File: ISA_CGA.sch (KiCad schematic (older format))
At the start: 15 parts, among them U1 74S112, U12 74LS393, U13 74LS08, U14 74LS32, U28 74LS10, U29 74S04, U3 74S86, U30 74LS32, U31 74S08, U42 74LS86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

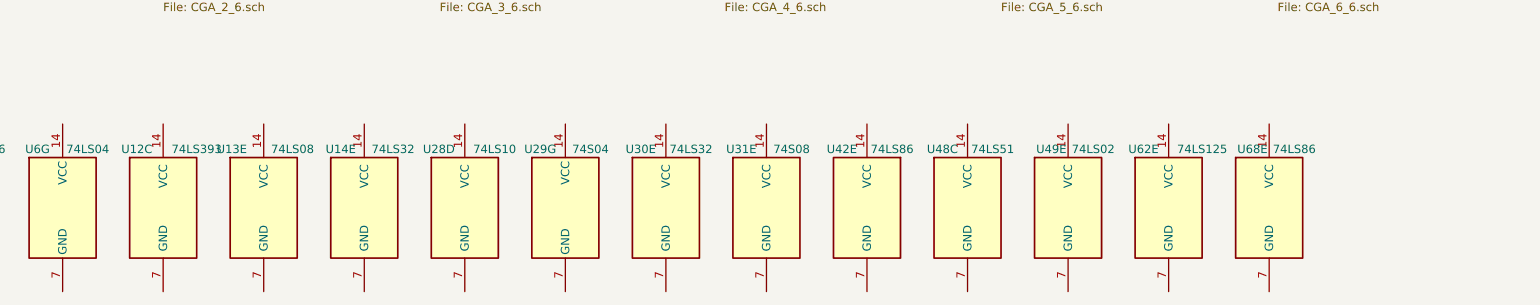
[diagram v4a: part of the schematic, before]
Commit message: Power connection for more units
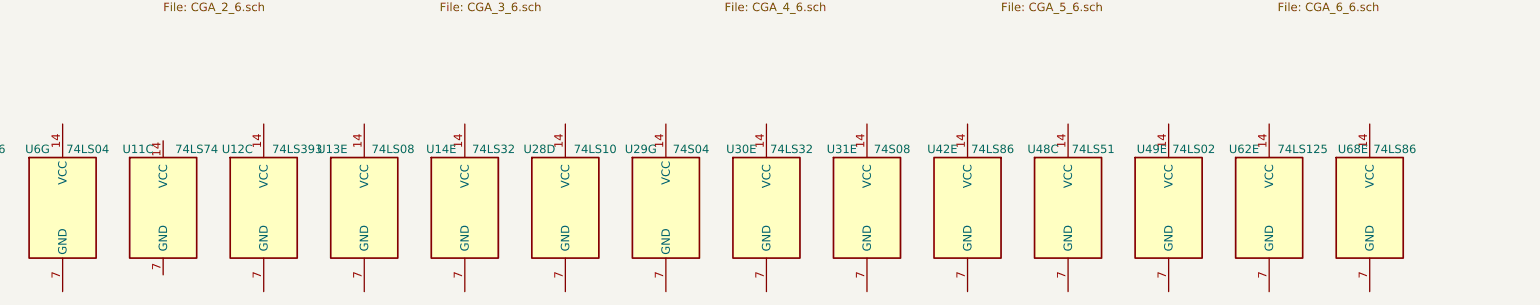
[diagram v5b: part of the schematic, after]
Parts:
- added U11: 74LS74, Package_DIP:DIP-14_W7.62mm_LongPads, symbol 74xx:74LS74
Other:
- moved on the sheet: U12C, U13E, U14E, U28D, U29G, U30E, U31E, U42E, U48C, U49E, U62E, U68E
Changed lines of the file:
@@
 L 74xx:74LS51 U?
 U 3 1 604901DC
-P 7500 3350
+P 8100 3350
 AR Path="/60463BAE/604901DC" Ref="U?"  Part="1"
 AR Path="/604901DC" Ref="U48"  Part="3"
-F 0 "U48" H 7350 3700 50  0000 C CNN
-F 1 "74LS51" H 7650 3700 50  0000 C CNN
-F 2 "Package_DIP:DIP-14_W7.62mm_LongPads" H 7500 3350 50  0001 C CNN
-F 3 "http://www.ti.com/lit/ds/symlink/sn74ls51.pdf" H 7500 3350 50  0001 C CNN
-	3    7500 3350
+F 0 "U48" H 7950 3700 50  0000 C CNN
+F 1 "74LS51" H 8250 3700 50  0000 C CNN
+F 2 "Package_DIP:DIP-14_W7.62mm_LongPads" H 8100 3350 50  0001 C CNN
+F 3 "http://www.ti.com/lit/ds/symlink/sn74ls51.pdf" H 8100 3350 50  0001 C CNN
+	3    8100 3350
 	1    0    0    -1
 $EndComp
@@
 L 74xx:74LS02 U?
 U 5 1 60495092
-P 8100 3350
+P 8700 3350
 AR Path="/60463BAE/60495092" Ref="U?"  Part="3"
 AR Path="/60495092" Ref="U49"  Part="5"
-F 0 "U49" H 8000 3700 50  0000 C CNN
-F 1 "74LS02" H 8250 3700 50  0000 C CNN
-F 2 "" H 8100 3350 50  0001 C CNN
-F 3 "http://www.ti.com/lit/gpn/sn74ls02" H 8100 3350 50  0001 C CNN
-	5    8100 3350
+F 0 "U49" H 8600 3700 50  0000 C CNN
+F 1 "74LS02" H 8850 3700 50  0000 C CNN
+F 2 "" H 8700 3350 50  0001 C CNN
+F 3 "http://www.ti.com/lit/gpn/sn74ls02" H 8700 3350 50  0001 C CNN
+	5    8700 3350
 	1    0    0    -1
 $EndComp
@@
 L 74xx:74LS125 U?
 U 5 1 6049EC67
-P 8700 3350
+P 9300 3350
 AR Path="/60463BAE/6049EC67" Ref="U?"  Part="1"
 AR Path="/6049EC67" Ref="U62"  Part="5"
-F 0 "U62" H 8550 3700 50  0000 C CNN
-F 1 "74LS125" H 8900 3700 50  0000 C CNN
-F 2 "Package_DIP:DIP-14_W10.16mm_LongPads" H 8700 3350 50  0001 C CNN
-F 3 "http://www.ti.com/lit/gpn/sn74LS125" H 8700 3350 50  0001 C CNN
-	5    8700 3350
+F 0 "U62" H 9150 3700 50  0000 C CNN
+F 1 "74LS125" H 9500 3700 50  0000 C CNN
+F 2 "Package_DIP:DIP-14_W10.16mm_LongPads" H 9300 3350 50  0001 C CNN
+F 3 "http://www.ti.com/lit/gpn/sn74LS125" H 9300 3350 50  0001 C CNN
+	5    9300 3350
 	1    0    0    -1
 $EndComp
@@
 L 74xx:74LS08 U?
 U 5 1 60735FFE
-P 3300 3350
+P 3900 3350
 AR Path="/60463BAE/60735FFE" Ref="U?"  Part="4"
 AR Path="/60735FFE" Ref="U13"  Part="5"
-F 0 "U13" H 3200 3700 50  0000 R CNN
-F 1 "74LS08" H 3600 3700 50  0000 R CNN
-F 2 "Package_DIP:DIP-14_W7.62mm_LongPads" H 3300 3350 50  0001 C CNN
-F 3 "http://www.ti.com/lit/gpn/sn74LS08" H 3300 3350 50  0001 C CNN
-	5    3300 3350
+F 0 "U13" H 3800 3700 50  0000 R CNN
+F 1 "74LS08" H 4200 3700 50  0000 R CNN
+F 2 "Package_DIP:DIP-14_W7.62mm_LongPads" H 3900 3350 50  0001 C CNN
+F 3 "http://www.ti.com/lit/gpn/sn74LS08" H 3900 3350 50  0001 C CNN
+	5    3900 3350
 	1    0    0    -1
 $EndComp
@@
 L 74xx:74LS10 U?
 U 4 1 6073B547
-P 4500 3350
+P 5100 3350
 AR Path="/60463BAE/6073B547" Ref="U?"  Part="3"
 AR Path="/6073B547" Ref="U28"  Part="4"
-F 0 "U28" H 4250 3700 50  0000 L CNN
-F 1 "74LS10" H 4550 3700 50  0000 L CNN
-F 2 "Package_DIP:DIP-14_W7.62mm_LongPads" H 4500 3350 50  0001 C CNN
-F 3 "http://www.ti.com/lit/gpn/sn74LS10" H 4500 3350 50  0001 C CNN
-	4    4500 3350
+F 0 "U28" H 4850 3700 50  0000 L CNN
+F 1 "74LS10" H 5150 3700 50  0000 L CNN
+F 2 "Package_DIP:DIP-14_W7.62mm_LongPads" H 5100 3350 50  0001 C CNN
+F 3 "http://www.ti.com/lit/gpn/sn74LS10" H 5100 3350 50  0001 C CNN
+	4    5100 3350
 	1    0    0    -1
 $EndComp
@@
 L 74xx:74LS32 U?
 U 5 1 607513C2
-P 3900 3350
+P 4500 3350
 AR Path="/60463BAE/607513C2" Ref="U?"  Part="2"
 AR Path="/607513C2" Ref="U14"  Part="5"
-F 0 "U14" H 3850 3700 50  0000 R CNN
-F 1 "74LS32" H 4200 3700 50  0000 R CNN
-F 2 "Package_DIP:DIP-14_W7.62mm_LongPads" H 3900 3350 50  0001 C CNN
-F 3 "http://www.ti.com/lit/gpn/sn74LS32" H 3900 3350 50  0001 C CNN
-	5    3900 3350
+F 0 "U14" H 4450 3700 50  0000 R CNN
+F 1 "74LS32" H 4800 3700 50  0000 R CNN
+F 2 "Package_DIP:DIP-14_W7.62mm_LongPads" H 4500 3350 50  0001 C CNN
+F 3 "http://www.ti.com/lit/gpn/sn74LS32" H 4500 3350 50  0001 C CNN
+	5    4500 3350
 	1    0    0    -1
 $EndComp
@@
 L 74xx:74LS86 U?
 U 5 1 61CD3D2F
-P 9300 3350
+P 9900 3350
 AR Path="/60463C10/61CD3D2F" Ref="U?"  Part="4"
 AR Path="/61CD3D2F" Ref="U68"  Part="5"
-F 0 "U68" H 9200 3700 50  0000 C CNN
-F 1 "74LS86" H 9450 3700 50  0000 C CNN
-F 2 "Package_DIP:DIP-14_W7.62mm_LongPads" H 9300 3350 50  0001 C CNN
-F 3 "74xx/74ls86.pdf" H 9300 3350 50  0001 C CNN
-	5    9300 3350
+F 0 "U68" H 9800 3700 50  0000 C CNN
+F 1 "74LS86" H 10050 3700 50  0000 C CNN
+F 2 "Package_DIP:DIP-14_W7.62mm_LongPads" H 9900 3350 50  0001 C CNN
+F 3 "74xx/74ls86.pdf" H 9900 3350 50  0001 C CNN
+	5    9900 3350
 	1    0    0    -1
 $EndComp
@@
 L 74xx:74LS08 U?
 U 5 1 61D13A76
-P 6300 3350
+P 6900 3350
 AR Path="/60463C10/61D13A76" Ref="U?"  Part="3"
 AR Path="/61D13A76" Ref="U31"  Part="5"
-F 0 "U31" H 6150 3700 50  0000 C CNN
-F 1 "74S08" H 6450 3700 50  0000 C CNN
-F 2 "Package_DIP:DIP-14_W7.62mm_LongPads" H 6300 3350 50  0001 C CNN
-F 3 "http://www.ti.com/lit/gpn/sn74LS08" H 6300 3350 50  0001 C CNN
-	5    6300 3350
+F 0 "U31" H 6750 3700 50  0000 C CNN
+F 1 "74S08" H 7050 3700 50  0000 C CNN
+F 2 "Package_DIP:DIP-14_W7.62mm_LongPads" H 6900 3350 50  0001 C CNN
+F 3 "http://www.ti.com/lit/gpn/sn74LS08" H 6900 3350 50  0001 C CNN
+	5    6900 3350
 	1    0    0    -1
 $EndComp
@@
 L 74xx:74LS86 U?
 U 5 1 629C2DFD
-P 6900 3350
+P 7500 3350
 AR Path="/60463C10/629C2DFD" Ref="U?"  Part="4"
 AR Path="/60463C57/629C2DFD" Ref="U?"  Part="1"
 AR Path="/629C2DFD" Ref="U42"  Part="5"
-F 0 "U42" H 7050 3700 50  0000 C CNN
-F 1 "74LS86" H 6750 3700 50  0000 C CNN
-F 2 "Package_DIP:DIP-14_W7.62mm_LongPads" H 6900 3350 50  0001 C CNN
-F 3 "74xx/74ls86.pdf" H 6900 3350 50  0001 C CNN
-	5    6900 3350
+F 0 "U42" H 7650 3700 50  0000 C CNN
+F 1 "74LS86" H 7350 3700 50  0000 C CNN
+F 2 "Package_DIP:DIP-14_W7.62mm_LongPads" H 7500 3350 50  0001 C CNN
+F 3 "74xx/74ls86.pdf" H 7500 3350 50  0001 C CNN
+	5    7500 3350
 	-1   0    0    -1
 $EndComp
@@
 L 74xx:74LS04 U?
 U 7 1 62A8BC3C
-P 5100 3350
+P 5700 3350
 AR Path="/60463C57/62A8BC3C" Ref="U?"  Part="6"
 AR Path="/62A8BC3C" Ref="U29"  Part="7"
-F 0 "U29" H 4950 3700 50  0000 C CNN
-F 1 "74S04" H 5250 3700 50  0000 C CNN
-F 2 "Package_DIP:DIP-14_W7.62mm_LongPads" H 5100 3350 50  0001 C CNN
-F 3 "http://www.ti.com/lit/gpn/sn74LS04" H 5100 3350 50  0001 C CNN
-	7    5100 3350
+F 0 "U29" H 5550 3700 50  0000 C CNN
+F 1 "74S04" H 5850 3700 50  0000 C CNN
+F 2 "Package_DIP:DIP-14_W7.62mm_LongPads" H 5700 3350 50  0001 C CNN
+F 3 "http://www.ti.com/lit/gpn/sn74LS04" H 5700 3350 50  0001 C CNN
+	7    5700 3350
 	1    0    0    -1
 $EndComp
@@
 L 74xx:74LS32 U?
 U 5 1 62AC6F3C
-P 5700 3350
+P 6300 3350
 AR Path="/60463C57/62AC6F3C" Ref="U?"  Part="3"
 AR Path="/62AC6F3C" Ref="U30"  Part="5"
-F 0 "U30" H 5550 3700 50  0000 C CNN
-F 1 "74LS32" H 5850 3700 50  0000 C CNN
-F 2 "" H 5700 3350 50  0001 C CNN
-F 3 "http://www.ti.com/lit/gpn/sn74LS32" H 5700 3350 50  0001 C CNN
-	5    5700 3350
+F 0 "U30" H 6150 3700 50  0000 C CNN
+F 1 "74LS32" H 6450 3700 50  0000 C CNN
+F 2 "" H 6300 3350 50  0001 C CNN
+F 3 "http://www.ti.com/lit/gpn/sn74LS32" H 6300 3350 50  0001 C CNN
+	5    6300 3350
 	1    0    0    -1
 $EndComp
@@
 L 74xx:74LS393 U?
 U 3 1 62B28623
-P 2700 3350
+P 3300 3350
 AR Path="/60463C57/62B28623" Ref="U?"  Part="1"
 AR Path="/62B28623" Ref="U12"  Part="3"
-F 0 "U12" H 2450 3700 50  0000 L CNN
-F 1 "74LS393" H 2750 3700 50  0000 L CNN
+F 0 "U12" H 3050 3700 50  0000 L CNN
+F 1 "74LS393" H 3350 3700 50  0000 L CNN
+F 2 "Package_DIP:DIP-14_W7.62mm_LongPads" H 3300 3350 50  0001 C CNN
+F 3 "74xx\\74LS393.pdf" H 3300 3350 50  0001 C CNN
+	3    3300 3350
+	1    0    0    -1
+$EndComp
+$Comp
+L 74xx:74LS74 U?
+U 3 1 62B87292
+P 2700 3350
+AR Path="/60463C57/62B87292" Ref="U?"  Part="2"
+AR Path="/62B87292" Ref="U11"  Part="3"
+F 0 "U11" H 2550 3700 50  0000 C CNN
+F 1 "74LS74" H 2900 3700 50  0000 C CNN
 F 2 "Package_DIP:DIP-14_W7.62mm_LongPads" H 2700 3350 50  0001 C CNN
-F 3 "74xx\\74LS393.pdf" H 2700 3350 50  0001 C CNN
+F 3 "74xx/74hc_hct74.pdf" H 2700 3350 50  0001 C CNN
 	3    2700 3350
 	1    0    0    -1

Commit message: more sheets
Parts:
- added U15: 74LS00, Package_DIP:DIP-14_W7.62mm_LongPads, symbol 74xx:74LS00
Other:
- moved on the sheet: U28D, U29G, U30E, U31E, U42E, U48C, U49E, U62E, U68E
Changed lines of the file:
@@
 L 74xx:74LS51 U?
 U 3 1 604901DC
-P 8100 3350
+P 8750 3350
 AR Path="/60463BAE/604901DC" Ref="U?"  Part="1"
 AR Path="/604901DC" Ref="U48"  Part="3"
-F 0 "U48" H 7950 3700 50  0000 C CNN
-F 1 "74LS51" H 8250 3700 50  0000 C CNN
-F 2 "Package_DIP:DIP-14_W7.62mm_LongPads" H 8100 3350 50  0001 C CNN
-F 3 "http://www.ti.com/lit/ds/symlink/sn74ls51.pdf" H 8100 3350 50  0001 C CNN
-	3    8100 3350
+F 0 "U48" H 8600 3700 50  0000 C CNN
+F 1 "74LS51" H 8900 3700 50  0000 C CNN
+F 2 "Package_DIP:DIP-14_W7.62mm_LongPads" H 8750 3350 50  0001 C CNN
+F 3 "http://www.ti.com/lit/ds/symlink/sn74ls51.pdf" H 8750 3350 50  0001 C CNN
+	3    8750 3350
 	1    0    0    -1
 $EndComp
@@
 L 74xx:74LS02 U?
 U 5 1 60495092
-P 8700 3350
+P 9350 3350
 AR Path="/60463BAE/60495092" Ref="U?"  Part="3"
 AR Path="/60495092" Ref="U49"  Part="5"
-F 0 "U49" H 8600 3700 50  0000 C CNN
-F 1 "74LS02" H 8850 3700 50  0000 C CNN
-F 2 "" H 8700 3350 50  0001 C CNN
-F 3 "http://www.ti.com/lit/gpn/sn74ls02" H 8700 3350 50  0001 C CNN
-	5    8700 3350
+F 0 "U49" H 9250 3700 50  0000 C CNN
+F 1 "74LS02" H 9500 3700 50  0000 C CNN
+F 2 "" H 9350 3350 50  0001 C CNN
+F 3 "http://www.ti.com/lit/gpn/sn74ls02" H 9350 3350 50  0001 C CNN
+	5    9350 3350
 	1    0    0    -1
 $EndComp
@@
 L 74xx:74LS125 U?
 U 5 1 6049EC67
-P 9300 3350
+P 9950 3350
 AR Path="/60463BAE/6049EC67" Ref="U?"  Part="1"
 AR Path="/6049EC67" Ref="U62"  Part="5"
-F 0 "U62" H 9150 3700 50  0000 C CNN
-F 1 "74LS125" H 9500 3700 50  0000 C CNN
-F 2 "Package_DIP:DIP-14_W10.16mm_LongPads" H 9300 3350 50  0001 C CNN
-F 3 "http://www.ti.com/lit/gpn/sn74LS125" H 9300 3350 50  0001 C CNN
-	5    9300 3350
+F 0 "U62" H 9800 3700 50  0000 C CNN
+F 1 "74LS125" H 10150 3700 50  0000 C CNN
+F 2 "Package_DIP:DIP-14_W10.16mm_LongPads" H 9950 3350 50  0001 C CNN
+F 3 "http://www.ti.com/lit/gpn/sn74LS125" H 9950 3350 50  0001 C CNN
+	5    9950 3350
 	1    0    0    -1
 $EndComp
@@
 L 74xx:74LS10 U?
 U 4 1 6073B547
-P 5100 3350
+P 5750 3350
 AR Path="/60463BAE/6073B547" Ref="U?"  Part="3"
 AR Path="/6073B547" Ref="U28"  Part="4"
-F 0 "U28" H 4850 3700 50  0000 L CNN
-F 1 "74LS10" H 5150 3700 50  0000 L CNN
-F 2 "Package_DIP:DIP-14_W7.62mm_LongPads" H 5100 3350 50  0001 C CNN
-F 3 "http://www.ti.com/lit/gpn/sn74LS10" H 5100 3350 50  0001 C CNN
-	4    5100 3350
+F 0 "U28" H 5500 3700 50  0000 L CNN
+F 1 "74LS10" H 5800 3700 50  0000 L CNN
+F 2 "Package_DIP:DIP-14_W7.62mm_LongPads" H 5750 3350 50  0001 C CNN
+F 3 "http://www.ti.com/lit/gpn/sn74LS10" H 5750 3350 50  0001 C CNN
+	4    5750 3350
 	1    0    0    -1
 $EndComp
@@
 L 74xx:74LS86 U?
 U 5 1 61CD3D2F
-P 9900 3350
+P 10550 3350
 AR Path="/60463C10/61CD3D2F" Ref="U?"  Part="4"
 AR Path="/61CD3D2F" Ref="U68"  Part="5"
-F 0 "U68" H 9800 3700 50  0000 C CNN
-F 1 "74LS86" H 10050 3700 50  0000 C CNN
-F 2 "Package_DIP:DIP-14_W7.62mm_LongPads" H 9900 3350 50  0001 C CNN
-F 3 "74xx/74ls86.pdf" H 9900 3350 50  0001 C CNN
-	5    9900 3350
+F 0 "U68" H 10450 3700 50  0000 C CNN
+F 1 "74LS86" H 10700 3700 50  0000 C CNN
+F 2 "Package_DIP:DIP-14_W7.62mm_LongPads" H 10550 3350 50  0001 C CNN
+F 3 "74xx/74ls86.pdf" H 10550 3350 50  0001 C CNN
+	5    10550 3350
 	1    0    0    -1
 $EndComp
@@
 L 74xx:74LS08 U?
 U 5 1 61D13A76
-P 6900 3350
+P 7550 3350
 AR Path="/60463C10/61D13A76" Ref="U?"  Part="3"
 AR Path="/61D13A76" Ref="U31"  Part="5"
-F 0 "U31" H 6750 3700 50  0000 C CNN
-F 1 "74S08" H 7050 3700 50  0000 C CNN
-F 2 "Package_DIP:DIP-14_W7.62mm_LongPads" H 6900 3350 50  0001 C CNN
-F 3 "http://www.ti.com/lit/gpn/sn74LS08" H 6900 3350 50  0001 C CNN
-	5    6900 3350
+F 0 "U31" H 7400 3700 50  0000 C CNN
+F 1 "74S08" H 7700 3700 50  0000 C CNN
+F 2 "Package_DIP:DIP-14_W7.62mm_LongPads" H 7550 3350 50  0001 C CNN
+F 3 "http://www.ti.com/lit/gpn/sn74LS08" H 7550 3350 50  0001 C CNN
+	5    7550 3350
 	1    0    0    -1
 $EndComp
@@
 L 74xx:74LS86 U?
 U 5 1 629C2DFD
-P 7500 3350
+P 8150 3350
 AR Path="/60463C10/629C2DFD" Ref="U?"  Part="4"
 AR Path="/60463C57/629C2DFD" Ref="U?"  Part="1"
 AR Path="/629C2DFD" Ref="U42"  Part="5"
-F 0 "U42" H 7650 3700 50  0000 C CNN
-F 1 "74LS86" H 7350 3700 50  0000 C CNN
-F 2 "Package_DIP:DIP-14_W7.62mm_LongPads" H 7500 3350 50  0001 C CNN
-F 3 "74xx/74ls86.pdf" H 7500 3350 50  0001 C CNN
-	5    7500 3350
+F 0 "U42" H 8300 3700 50  0000 C CNN
+F 1 "74LS86" H 8000 3700 50  0000 C CNN
+F 2 "Package_DIP:DIP-14_W7.62mm_LongPads" H 8150 3350 50  0001 C CNN
+F 3 "74xx/74ls86.pdf" H 8150 3350 50  0001 C CNN
+	5    8150 3350
 	-1   0    0    -1
 $EndComp
@@
 L 74xx:74LS04 U?
 U 7 1 62A8BC3C
-P 5700 3350
+P 6350 3350
 AR Path="/60463C57/62A8BC3C" Ref="U?"  Part="6"
 AR Path="/62A8BC3C" Ref="U29"  Part="7"
-F 0 "U29" H 5550 3700 50  0000 C CNN
-F 1 "74S04" H 5850 3700 50  0000 C CNN
-F 2 "Package_DIP:DIP-14_W7.62mm_LongPads" H 5700 3350 50  0001 C CNN
-F 3 "http://www.ti.com/lit/gpn/sn74LS04" H 5700 3350 50  0001 C CNN
-	7    5700 3350
+F 0 "U29" H 6200 3700 50  0000 C CNN
+F 1 "74S04" H 6500 3700 50  0000 C CNN
+F 2 "Package_DIP:DIP-14_W7.62mm_LongPads" H 6350 3350 50  0001 C CNN
+F 3 "http://www.ti.com/lit/gpn/sn74LS04" H 6350 3350 50  0001 C CNN
+	7    6350 3350
 	1    0    0    -1
 $EndComp
@@
 L 74xx:74LS32 U?
 U 5 1 62AC6F3C
-P 6300 3350
+P 6950 3350
 AR Path="/60463C57/62AC6F3C" Ref="U?"  Part="3"
 AR Path="/62AC6F3C" Ref="U30"  Part="5"
-F 0 "U30" H 6150 3700 50  0000 C CNN
-F 1 "74LS32" H 6450 3700 50  0000 C CNN
-F 2 "" H 6300 3350 50  0001 C CNN
-F 3 "http://www.ti.com/lit/gpn/sn74LS32" H 6300 3350 50  0001 C CNN
-	5    6300 3350
+F 0 "U30" H 6800 3700 50  0000 C CNN
+F 1 "74LS32" H 7100 3700 50  0000 C CNN
+F 2 "" H 6950 3350 50  0001 C CNN
+F 3 "http://www.ti.com/lit/gpn/sn74LS32" H 6950 3350 50  0001 C CNN
+	5    6950 3350
 	1    0    0    -1
 $EndComp
@@
 AR Path="/62B28623" Ref="U12"  Part="3"
 F 0 "U12" H 3050 3700 50  0000 L CNN
-F 1 "74LS393" H 3350 3700 50  0000 L CNN
+F 1 "74LS393" H 3300 3700 50  0000 L CNN
 F 2 "Package_DIP:DIP-14_W7.62mm_LongPads" H 3300 3350 50  0001 C CNN
 F 3 "74xx\\74LS393.pdf" H 3300 3350 50  0001 C CNN
@@
 	1    0    0    -1
 $EndComp
+$Comp
+L 74xx:74LS00 U?
+U 5 1 62BBA7C0
+P 5100 3350
+AR Path="/60463C57/62BBA7C0" Ref="U?"  Part="4"
+AR Path="/62BBA7C0" Ref="U15"  Part="5"
+F 0 "U15" H 4900 3700 50  0000 L CNN
+F 1 "74LS00" H 5100 3700 50  0000 L CNN
+F 2 "Package_DIP:DIP-14_W7.62mm_LongPads" H 5100 3350 50  0001 C CNN
+F 3 "http://www.ti.com/lit/gpn/sn74ls00" H 5100 3350 50  0001 C CNN
+	5    5100 3350
+	1    0    0    -1
+$EndComp
